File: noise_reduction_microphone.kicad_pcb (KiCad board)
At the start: 4 copper layers, 103 x 60 mm, 37 parts, among them IC1 MMICT3902-00-012, IC2 MMICT3902-00-012, IC3 MMICT3902-00-012, IC4 MMICT3902-00-012, J1 Power/Audio, J2 Debug Header, U1 PCM5101A

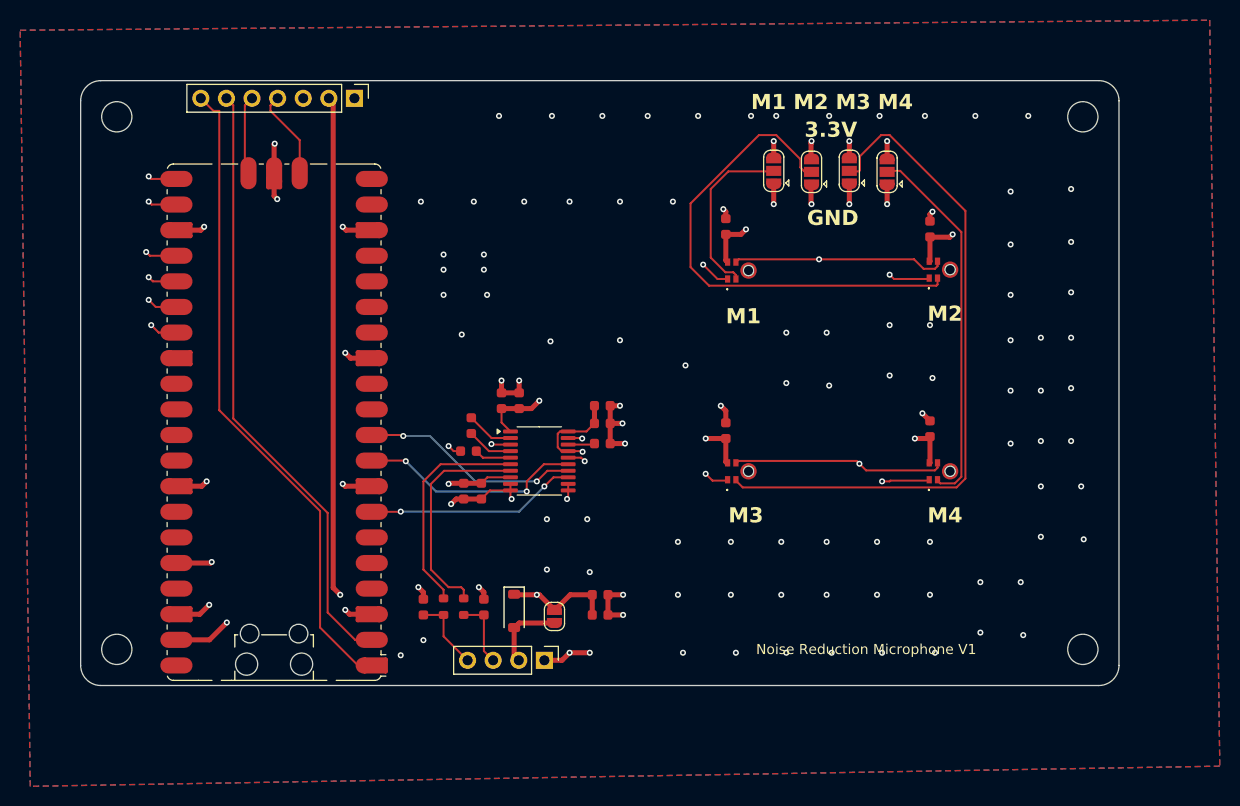
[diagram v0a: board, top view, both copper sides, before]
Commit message: Added test points and another connector for audio gnd
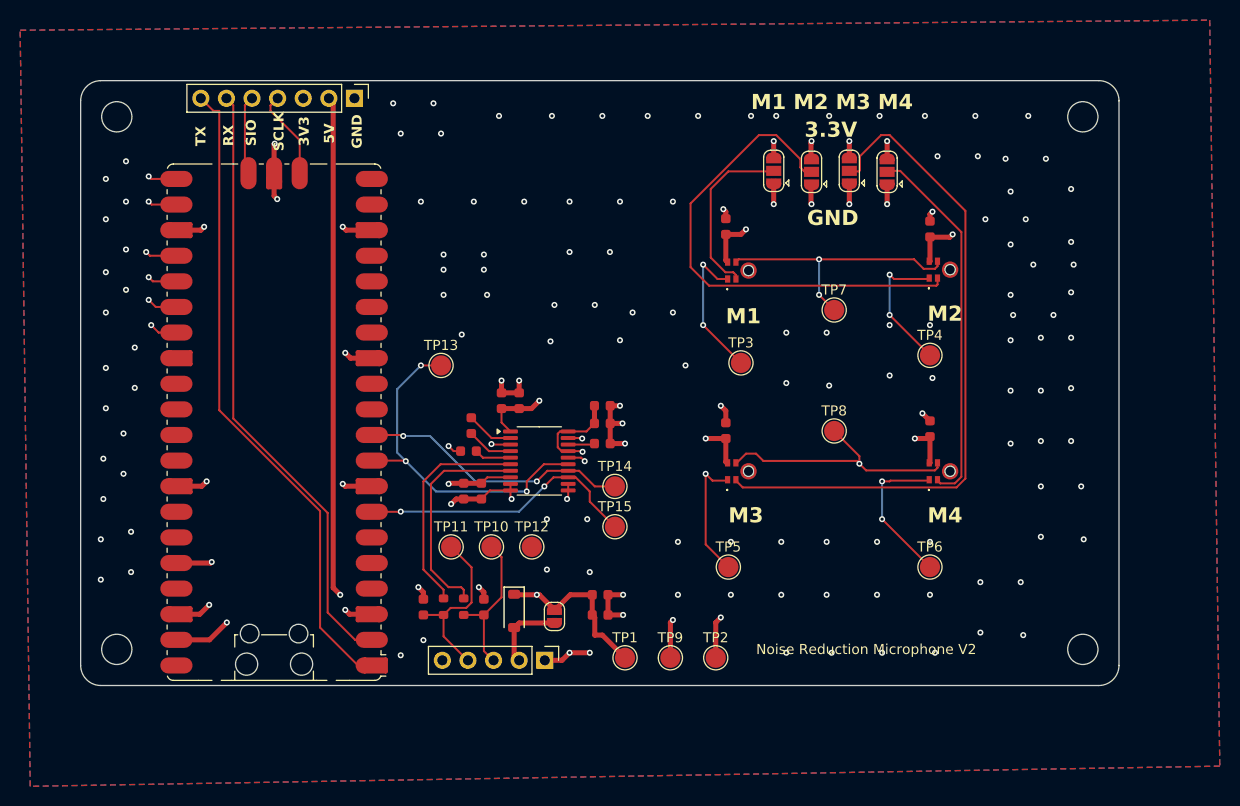
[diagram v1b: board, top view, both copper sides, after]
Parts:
- added TP1: 5V, TestPoint:TestPoint_Pad_D2.0mm, F.Cu at (125.0, 131.2)
- added TP10: AUDIO_R, TestPoint:TestPoint_Pad_D2.0mm, F.Cu at (111.8, 120.2)
- added TP11: AUDIO_L, TestPoint:TestPoint_Pad_D2.0mm, F.Cu at (107.8, 120.2)
- added TP12: AUDIO_GND, TestPoint:TestPoint_Pad_D2.0mm, F.Cu at (115.8, 120.2)
- added TP13: WS, TestPoint:TestPoint_Pad_D2.0mm, F.Cu at (106.8, 102.2)
- added TP14: DAC_DIN, TestPoint:TestPoint_Pad_D2.0mm, F.Cu at (124.0, 114.2)
- added TP15: BCLK, TestPoint:TestPoint_Pad_D2.0mm, F.Cu at (124.0, 118.2)
- added TP2: 3V, TestPoint:TestPoint_Pad_D2.0mm, F.Cu at (134.0, 131.2)
- added TP3: MIC1_OUT, TestPoint:TestPoint_Pad_D2.0mm, F.Cu at (136.5, 102.0)
- added TP4: MIC2_OUT, TestPoint:TestPoint_Pad_D2.0mm, F.Cu at (155.2, 101.2)
- added TP5: MIC3_OUT, TestPoint:TestPoint_Pad_D2.0mm, F.Cu at (135.2, 122.2)
- added TP6: MIC4_OUT, TestPoint:TestPoint_Pad_D2.0mm, F.Cu at (155.2, 122.2)
- added TP7: CLK1, TestPoint:TestPoint_Pad_D2.0mm, F.Cu at (145.8, 96.8)
- added TP8: CLK2, TestPoint:TestPoint_Pad_D2.0mm, F.Cu at (145.8, 108.8)
- added TP9: GND, TestPoint:TestPoint_Pad_D2.0mm, F.Cu at (129.5, 131.2)
- J1: footprint Connector_PinHeader_2.54mm:PinHeader_1x04_P2.54mm_Vertical -> Connector_PinHeader_2.54mm:PinHeader_1x05_P2.54mm_Vertical
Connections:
- A1 pad 13: GND -> AUDIO_GND
- A1 pad 18: GND -> AUDIO_GND
- A1 pad 23: GND -> AUDIO_GND
- A1 pad 28: GND -> AUDIO_GND
- A1 pad 3: GND -> AUDIO_GND
- A1 pad 33: GND -> AUDIO_GND
- A1 pad 38: GND -> AUDIO_GND
- A1 pad 8: GND -> AUDIO_GND
- A1 pad D2: GND -> AUDIO_GND
- C1 pad 2: GND -> AUDIO_GND
- C10 pad 1: GND -> AUDIO_GND
- C11 pad 2: GND -> AUDIO_GND
- C12 pad 2: GND -> AUDIO_GND
- C13 pad 2: GND -> AUDIO_GND
- C14 pad 2: GND -> AUDIO_GND
- C15 pad 2: GND -> AUDIO_GND
- C16 pad 2: GND -> AUDIO_GND
- C17 pad 2: GND -> AUDIO_GND
- C2 pad 2: GND -> AUDIO_GND
- C3 pad 2: GND -> AUDIO_GND
- C4 pad 2: GND -> AUDIO_GND
- C5 pad 2: GND -> AUDIO_GND
- C6 pad 2: GND -> AUDIO_GND
- C7 pad 2: GND -> AUDIO_GND
- C9 pad 2: GND -> AUDIO_GND
- IC1 pad 3: GND -> AUDIO_GND
- IC2 pad 3: GND -> AUDIO_GND
- IC3 pad 3: GND -> AUDIO_GND
- IC4 pad 3: GND -> AUDIO_GND
- J1 pad 1: GND -> AUDIO_GND
- J2 pad 1: GND -> AUDIO_GND
- JP2 pad 1: GND -> AUDIO_GND
- JP3 pad 1: GND -> AUDIO_GND
- JP4 pad 1: GND -> AUDIO_GND
- JP5 pad 1: GND -> AUDIO_GND
- U1 pad 10: GND -> AUDIO_GND
- U1 pad 11: GND -> AUDIO_GND
- U1 pad 12: GND -> AUDIO_GND
- U1 pad 16: GND -> AUDIO_GND
- U1 pad 19: GND -> AUDIO_GND
- U1 pad 3: GND -> AUDIO_GND
- U1 pad 9: GND -> AUDIO_GND
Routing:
- net AUDIO_GND: track 0.00 -> 84.3 mm, vias 0 -> 157
- net GND: track 80.4 -> 0.00 mm, vias 118 -> 0
- net WS: track 22.5 -> 35.3 mm, vias 2 -> 3
- net MIC1_DOUT: track 63.5 -> 74.8 mm, vias 2 -> 3
- net MIC4_DOUT: track 91.8 -> 102.3 mm, vias 2 -> 3
- net MIC3_DOUT: track 67.9 -> 78.1 mm
- net MIC2_DOUT: track 82.3 -> 92.0 mm, vias 2 -> 3
- net AUDIO_L: track 7.49 -> 17.1 mm
- net AUDIO_R: track 6.88 -> 14.8 mm
- net BCLK: track 20.9 -> 28.2 mm
- net 5V_Input: track 98.3 -> 104.3 mm
- net CLK1: track 93.8 -> 99.4 mm, vias 2 -> 3
- net DAC_DIN: track 21.8 -> 27.1 mm
- net CLK2: track 102.1 -> 107.0 mm
- net +3.3V: track 51.8 -> 56.0 mm, vias 12 -> 13
- added copper zone on B.Cu, net AUDIO_GND
- added copper zone on F.Cu, net AUDIO_GND
- added copper zone on In1.Cu, net AUDIO_GND
- removed copper zone on B.Cu, net GND
- removed copper zone on F.Cu, net GND
- removed copper zone on In1.Cu, net GND
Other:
- board text added: "3V3"
- board text added: "5V"
- board text added: "Noise Reduction Microphone V2"
- board text added: "RX"
- board text added: "SCLK"
- board text added: "SIO"
- board text added: "TX"
- board text removed: "Noise Reduction Microphone V1"
